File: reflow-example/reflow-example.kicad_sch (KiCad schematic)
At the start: 14 parts, among them U1 NE555D, U2 74LS163

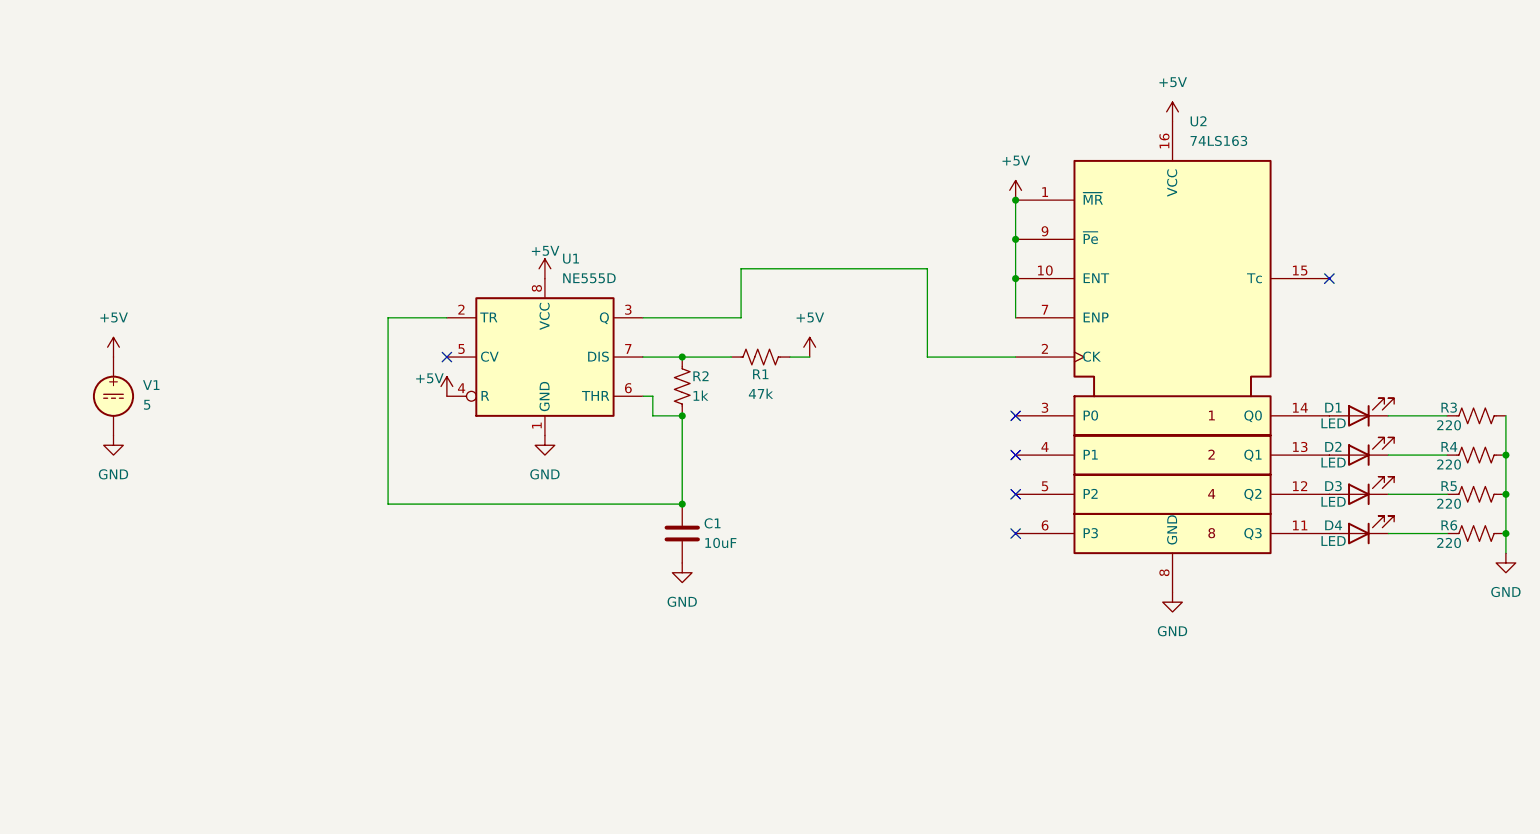
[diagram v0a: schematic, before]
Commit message: update schematic to use 7 segment displays
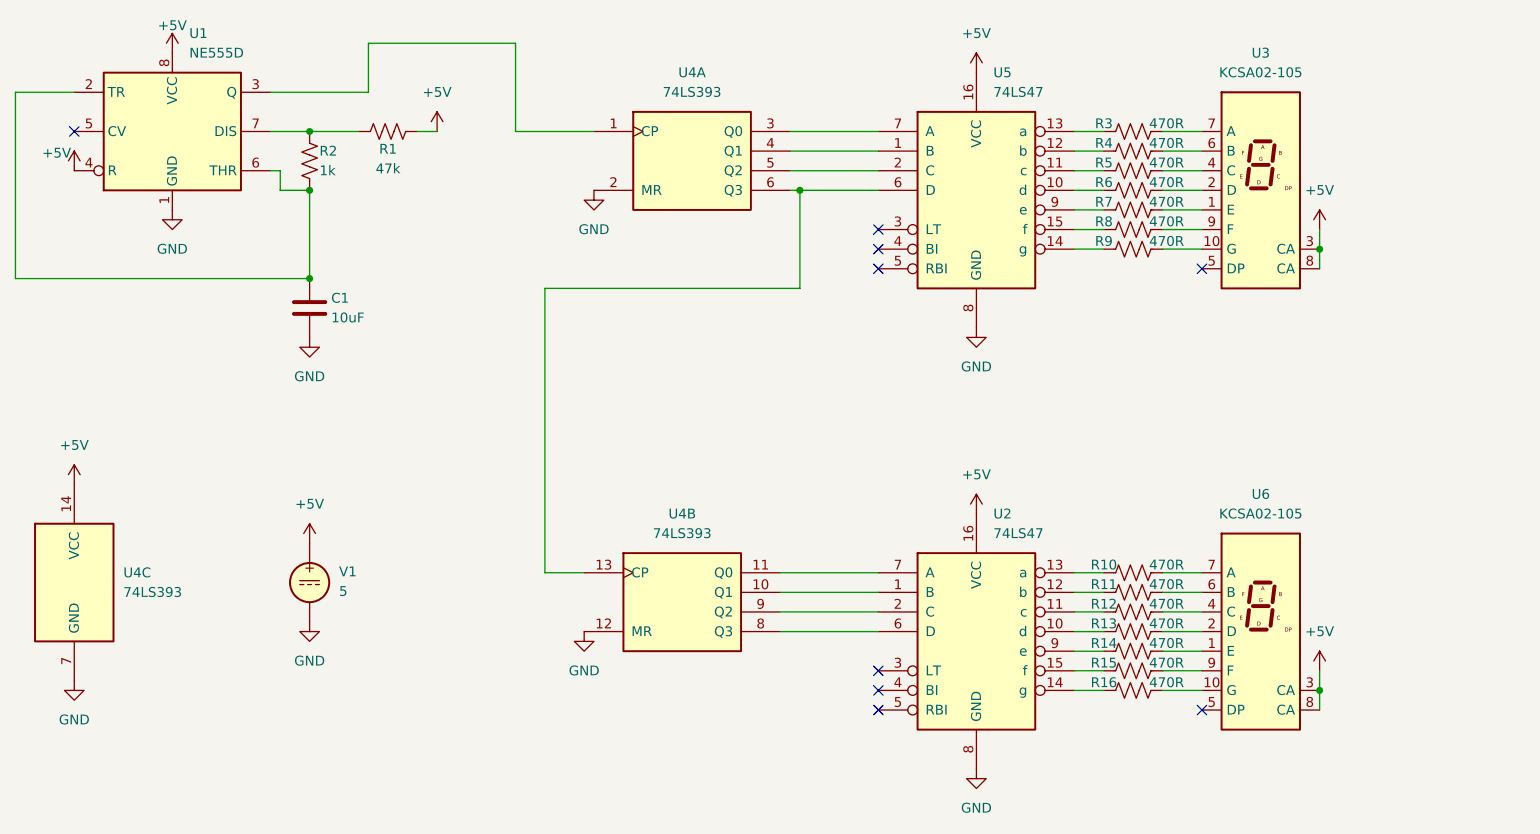
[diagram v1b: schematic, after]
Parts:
- removed D1, D2, D3, D4: LED, symbol Device:LED
- removed U2: 74LS163, symbol 74xx_IEEE:74LS163
- added R10, R11, R12, R13, R14, R15, R16, R7, R8, R9: 470R, symbol Device:R_US
- added U2, U5: 74LS47, symbol 74xx:74LS47
- added U3, U6: KCSA02-105, Display_7Segment:HDSP-7401, symbol Display_Character:KCSA02-105
- added U4: 74LS393, symbol 74xx:74LS393
- R3, R4, R5, R6: value 220 -> 470R
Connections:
- net +5V: now also U2.16 (VCC), U3.3 (CA), U3.8 (CA), U4.14 (VCC), U5.16 (VCC), U6.3 (CA), U6.8 (CA)
- net GND: now also U2.8 (GND), U4.12 (MR), U4.2 (MR), U4.7 (GND), U5.8 (GND); no longer R3.2, R4.2, R5.2, R6.2
- net at R4.1: now also U5.12 (b)
- net at R5.1: now also U5.11 (c)
- net at R6.1: now also U5.10 (d)
- net at U1.3 (Q): now also U4.1 (CP)
- net at R3.1: now also U5.13 (a)
- new net: U2.1 (B), U4.10 (Q1)
- new net: U2.7 (A), U4.11 (Q0)
- new net: U4.13 (CP), U4.6 (Q3), U5.6 (D)
- new net: U2.6 (D), U4.8 (Q3)
- new net: U2.2 (C), U4.9 (Q2)
- new net: R10.1, U2.13 (a)
- new net: R10.2, U6.7 (A)
- new net: R13.1, U2.10 (d)
- new net: R12.1, U2.11 (c)
- new net: R11.1, U2.12 (b)
- new net: R16.1, U2.14 (g)
- new net: R15.1, U2.15 (f)
- new net: R14.1, U2.9 (e)
- new net: R12.2, U6.4 (C)
- new net: R7.1, U5.9 (e)
- new net: R7.2, U3.1 (E)
- new net: R9.1, U5.14 (g)
- new net: R9.2, U3.10 (G)
- new net: R16.2, U6.10 (G)
- new net: R6.2, U3.2 (D)
- new net: R5.2, U3.4 (C)
- new net: R4.2, U3.6 (B)
- new net: R3.2, U3.7 (A)
- new net: R8.2, U3.9 (F)
- new net: R14.2, U6.1 (E)
- new net: R13.2, U6.2 (D)
- new net: R11.2, U6.6 (B)
- new net: R15.2, U6.9 (F)
- new net: U4.3 (Q0), U5.7 (A)
- new net: U4.4 (Q1), U5.1 (B)
- new net: U4.5 (Q2), U5.2 (C)
- new net: R8.1, U5.15 (f)
- no-connect marks 6 -> 9
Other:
- moved on the sheet: C1, R1, R2, U1, V1
